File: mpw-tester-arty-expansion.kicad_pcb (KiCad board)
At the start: 4 copper layers, 53.3 x 61.5 mm, 145 parts, among them J1 USB4105-GF-A, J10 61300211121, J11 61300211121, J12 61300211121, J14 61300311121, J15 61300311121, J18 61300411121, J19 61300711121, J20 61300411121, J3 arty_chipKIT_connector, J4 61300211121, J5 61300311121, J6 61300211121, J7 61300211121, J8 61300211121, J9 61300211121, M1 Arty_A7, Q1 DTC014TEBTL, SW1 JS202011JCQN, SW2 JS202011JCQN, SW3 JS202011JCQN, U1 SN74LVC1G125DCKR, U10 TPD4E02B04DQA, U2 FT232HQ, U3 SN74LVC1G125DCKR, U4 MAX811REUS+T, U5 NTS0102DP, U6 MCP4661-103E/ML, U7 Caravel_breakout_PCB, U8 W25Q32FVSS, U9 MIC2211-AAYML-TR, Y1 ABM8G-12.000MHZ-18-D2Y-T, Y2 ECS-2520MVLC-100-BN-TR

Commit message: Update PCB name, bump revision to 1.0.0
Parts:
- moved G*** 2.60 mm to (164.8, 73.8) (x2)
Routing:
- net /CRVL_XCLK: track 27.7 -> 26.8 mm
- net AGND: track 130.1 -> 130.7 mm, vias 61 -> 60
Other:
- board text added: "MPW tester Arty ext."
- board text added: "Rev. 1.0.0"
- board text removed: "MPW tester Arty"
- board text removed: "Rev. 0.0.99"
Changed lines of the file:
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@@
   (title_block
     (title "MPW tester Arty expansion")
-    (date "2022-12-02")
-    (rev "0.0.99")
+    (date "2022-12-12")
+    (rev "1.0.0")
   )
   (layers
@@
   )
   (footprint "antmicro-footprints:antmicro-logo_scaled_12mm_mask" (layer "F.Cu")
-    (at 167.4 73.8)
+    (at 164.8 73.75)
     (attr board_only exclude_from_pos_files exclude_from_bom)
     (fp_text reference "G***" (at 0.6096 -2.0955) (layer "F.SilkS") hide
@@
   )
   (footprint "antmicro-footprints:antmicro-logo_scaled_12mm" (layer "F.Cu")
-    (at 167.4 73.8)
+    (at 164.8 73.75)
     (attr board_only exclude_from_pos_files exclude_from_bom)
     (fp_text reference "G***" (at 0.6096 -2.0955) (layer "F.SilkS") hide
@@
   (gr_line (start 128.1 127.55) (end 125.55 125) (layer "Edge.Cuts") (width 0.1))
   (gr_line (start 174.8 125) (end 163.4 125) (layer "Edge.Cuts") (width 0.1))
-  (gr_text "Rev. 0.0.99" (at 165.1 76.9) (layer "F.Cu")
+  (gr_text "Rev. 1.0.0" (at 162.55 76.75) (layer "F.Cu")
     (effects (font (size 0.85 0.85) (thickness 0.18)) (justify left))
   )
-  (gr_text "MPW tester Arty" (at 165.1 75.5) (layer "F.Cu")
+  (gr_text "MPW tester Arty ext." (at 162.55 75.35) (layer "F.Cu")
     (effects (font (size 0.85 0.85) (thickness 0.18)) (justify left))
   )
@@
     (effects (font (size 0.7 0.7) (thickness 0.15)))
   )
-  (gr_text "Rev. 0.0.99" (at 165.1 76.9) (layer "F.Mask")
+  (gr_text "Rev. 1.0.0" (at 162.55 76.75) (layer "F.Mask")
     (effects (font (size 0.85 0.85) (thickness 0.18)) (justify left))
   )
-  (gr_text "MPW tester Arty" (at 165.1 75.5) (layer "F.Mask")
+  (gr_text "MPW tester Arty ext." (at 162.55 75.35) (layer "F.Mask")
     (effects (font (size 0.85 0.85) (thickness 0.18)) (justify left))
   )
@@
   (via (at 135.7 84.5) (size 0.6) (drill 0.3) (layers "F.Cu" "B.Cu") (net 1))
   (via (at 135.5 78.8) (size 0.6) (drill 0.3) (layers "F.Cu" "B.Cu") (net 1))
-  (via (at 159.9 73.5) (size 0.6) (drill 0.3) (layers "F.Cu" "B.Cu") (net 1))
   (via (at 129.7 84.4) (size 0.6) (drill 0.3) (layers "F.Cu" "B.Cu") (net 1))
   (via (at 134.2 73.6) (size 0.6) (drill 0.3) (layers "F.Cu" "B.Cu") (net 1))
@@
   (segment (start 139.15 109.55) (end 139.2 109.5) (width 0.2) (layer "B.Cu") (net 1))
   (segment (start 130.2 105) (end 130.2 106.43) (width 0.2) (layer "B.Cu") (net 1))
-  (segment (start 159.9 74.4) (end 159.9 73.5) (width 0.2) (layer "B.Cu") (net 1))
   (segment (start 136.65 115.15) (end 136.9 114.9) (width 0.2) (layer "B.Cu") (net 1))
   (segment (start 136.9 125.7) (end 136.9 126.6) (width 0.2) (layer "B.Cu") (net 1))
@@
   (segment (start 163.4 82.2) (end 163.3405 82.2) (width 0.2) (layer "B.Cu") (net 1))
   (segment (start 143.75 89.468) (end 143.75 90.368) (width 0.2) (layer "B.Cu") (net 1))
+  (segment (start 159.9 74.4) (end 159.9 75.9) (width 0.2) (layer "B.Cu") (net 1))
   (segment (start 135.7 83.6) (end 135.7 84.5) (width 0.2) (layer "B.Cu") (net 1))
   (segment (start 146.3 107.2) (end 147 107.75) (width 0.2) (layer "B.Cu") (net 1))
@@
   (segment (start 133.6 123.3) (end 133.6 124.5) (width 0.2) (layer "B.Cu") (net 3))
   (segment (start 123.9 103.9) (end 124.4 103.4) (width 0.2) (layer "B.Cu") (net 3))
-  (segment (start 128.9 75.6) (end 128.9 85.7) (width 0.2) (layer "F.Cu") (net 4))
+  (segment (start 129.4 75.1) (end 128.9 75.6) (width 0.2) (layer "F.Cu") (net 4))
+  (segment (start 158.1 73.5) (end 140.8 73.5) (width 0.2) (layer "F.Cu") (net 4))
   (segment (start 140.8 73.5) (end 139.2 75.1) (width 0.2) (layer "F.Cu") (net 4))
   (segment (start 139.2 75.1) (end 129.4 75.1) (width 0.2) (layer "F.Cu") (net 4))
-  (segment (start 129.4 75.1) (end 128.9 75.6) (width 0.2) (layer "F.Cu") (net 4))
-  (segment (start 158.5 73.5) (end 140.8 73.5) (width 0.2) (layer "F.Cu") (net 4))
+  (segment (start 128.9 75.6) (end 128.9 85.7) (width 0.2) (layer "F.Cu") (net 4))
   (via (at 128.9 85.7) (size 0.6) (drill 0.3) (layers "F.Cu" "B.Cu") (net 4))
-  (via (at 158.5 73.5) (size 0.6) (drill 0.3) (layers "F.Cu" "B.Cu") (net 4))
+  (via (at 158.1 73.5) (size 0.6) (drill 0.3) (layers "F.Cu" "B.Cu") (net 4))
   (segment (start 125.54 94.52) (end 127.98 94.52) (width 0.2) (layer "B.Cu") (net 4))
   (segment (start 127.3 93.7) (end 127.3 86.2) (width 0.2) (layer "B.Cu") (net 4))
@@
   (segment (start 158.9 76.7) (end 157.9 76.7) (width 0.2) (layer "B.Cu") (net 4))
   (segment (start 127.8 85.7) (end 128.9 85.7) (width 0.2) (layer "B.Cu") (net 4))
+  (segment (start 158.5 74.4) (end 158.5 73.9) (width 0.2) (layer "B.Cu") (net 4))
   (segment (start 157.5 76.3) (end 156.6 76.3) (width 0.2) (layer "B.Cu") (net 4))
   (segment (start 128 94.5) (end 128 94.4) (width 0.2) (layer "B.Cu") (net 4))
+  (segment (start 158.5 73.9) (end 158.1 73.5) (width 0.2) (layer "B.Cu") (net 4))
   (segment (start 156.425 74.125) (end 156.7 74.4) (width 0.2) (layer "B.Cu") (net 4))
   (segment (start 128 94.4) (end 127.3 93.7) (width 0.2) (layer "B.Cu") (net 4))
   (segment (start 159.2 76.4) (end 158.9 76.7) (width 0.2) (layer "B.Cu") (net 4))
-  (segment (start 158.5 74.4) (end 158.5 73.5) (width 0.2) (layer "B.Cu") (net 4))
   (segment (start 156.6 76.3) (end 156.425 76.475) (width 0.2) (layer "B.Cu") (net 4))
   (segment (start 127.98 94.52) (end 128 94.5) (width 0.2) (layer "B.Cu") (net 4))
@@
   (via (at 146.95 90.368) (size 0.6) (drill 0.3) (layers "F.Cu" "B.Cu") (net 8))
   (via (at 162.7 84.2) (size 0.6) (drill 0.3) (layers "F.Cu" "B.Cu") (net 8))
-  (via (at 160.5 71.7) (size 0.6) (drill 0.3) (layers "F.Cu" "B.Cu") (net 8))
   (via (at 142 74.4) (size 0.6) (drill 0.3) (layers "F.Cu" "B.Cu") (net 8))
   (via (at 151.75 90.368) (size 0.6) (drill 0.3) (layers "F.Cu" "B.Cu") (net 8))
   (via (at 133.2 76.75) (size 0.6) (drill 0.3) (layers "F.Cu" "B.Cu") (net 8))
+  (via (at 160.7 71) (size 0.6) (drill 0.3) (layers "F.Cu" "B.Cu") (net 8))
   (via (at 153.35 90.368) (size 0.6) (drill 0.3) (layers "F.Cu" "B.Cu") (net 8))
   (segment (start 151.25 108.6) (end 152.3 108.6) (width 0.2) (layer "B.Cu") (net 8))
@@
   (segment (start 153.8 67) (end 152.81 67) (width 0.2) (layer "B.Cu") (net 8))
   (segment (start 171.8 74.205) (end 173.405 74.205) (width 0.2) (layer "B.Cu") (net 8))
+  (segment (start 161.3 71.7) (end 161.3 71.6) (width 0.15) (layer "B.Cu") (net 8))
   (segment (start 148.55 89.468) (end 148.55 90.368) (width 0.2) (layer "B.Cu") (net 8))
   (segment (start 155.25 108.6) (end 155.25 108.15) (width 0.2) (layer "B.Cu") (net 8))
@@
   (segment (start 155.5 107.9) (end 156.2 107.9) (width 0.2) (layer "B.Cu") (net 8))
   (segment (start 142.9 74.4) (end 142 74.4) (width 0.2) (layer "B.Cu") (net 8))
-  (segment (start 161.3 71.7) (end 160.5 71.7) (width 0.2) (layer "B.Cu") (net 8))
+  (segment (start 161.3 71.6) (end 160.7 71) (width 0.15) (layer "B.Cu") (net 8))
   (segment (start 175 73) (end 174.3 73.7) (width 0.2) (layer "B.Cu") (net 8))
   (segment (start 163.3 83.6) (end 162.7 84.2) (width 0.2) (layer "B.Cu") (net 8))
@@
   (segment (start 147.775 84.578) (end 147.775 81.175) (width 0.2) (layer "F.Cu") (net 51))
   (segment (start 147.775 84.578) (end 147.775 86.128) (width 0.2) (layer "F.Cu") (net 51))
-  (segment (start 147.2 77.4) (end 164.1 77.4) (width 0.182) (layer "F.Cu") (net 51))
-  (segment (start 164.455 77.755) (end 164.455 78.9) (width 0.182) (layer "F.Cu") (net 51))
+  (segment (start 163.155 77.6) (end 147.2 77.6) (width 0.182) (layer "F.Cu") (net 51))
+  (segment (start 147.2 77.6) (end 146.94 77.86) (width 0.182) (layer "F.Cu") (net 51))
   (segment (start 146.94 80.34) (end 147.775 81.175) (width 0.2) (layer "F.Cu") (net 51))
-  (segment (start 164.1 77.4) (end 164.455 77.755) (width 0.182) (layer "F.Cu") (net 51))
-  (segment (start 146.94 78.9) (end 146.94 77.66) (width 0.182) (layer "F.Cu") (net 51))
-  (segment (start 146.94 77.66) (end 147.2 77.4) (width 0.182) (layer "F.Cu") (net 51))
+  (segment (start 146.94 77.86) (end 146.94 78.9) (width 0.182) (layer "F.Cu") (net 51))
+  (segment (start 164.455 78.9) (end 163.155 77.6) (width 0.182) (layer "F.Cu") (net 51))
   (segment (start 144.375 76.425) (end 144.4 76.45) (width 0.182) (layer "B.Cu") (net 52))
   (segment (start 144.4 76.45) (end 144.4 78.9) (width 0.182) (layer "B.Cu") (net 52))

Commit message: Removed Arty A7 model
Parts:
- removed M1: Arty_A7, antmicro-footprints:ARTY_A7
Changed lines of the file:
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@@
       ) (layer "F.Mask") (width 0.01) (fill solid))
-  )
-  (footprint "antmicro-footprints:ARTY_A7" (layer "F.Cu")
-    (at 150 100)
-    (property "MPN" "410-319")
-    (property "Manufacturer" "Digilent")
-    (property "Sheetfile" "mpw-tester-arty-expansion.kicad_sch")
-    (property "Sheetname" "")
-    (property "exclude_from_bom" "")
-    (attr exclude_from_bom)
-    (fp_text reference "M1" (at 0 -0.5 unlocked) (layer "F.SilkS") hide
-      (effects (font (size 0.65 0.65) (thickness 0.15)))
-    )
-    (fp_text value "Arty_A7" (at 0 1 unlocked) (layer "F.Fab") hide
-      (effects (font (size 0.65 0.65) (thickness 0.15)))
-    )
-    (model "${ANT3DMDL}/Arty Rev C.stp"
-      (offset (xyz 0.55 24.6 -13.2))
-      (scale (xyz 1 1 1))
-      (rotate (xyz 0 0 90))
-    )
   )
   (footprint "mpw-tester-arty-expansion-footprints:ARTY_A7_SHIELD" locked (layer "F.Cu")

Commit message: Corrected deadbeef signage
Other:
- board text added: "PCB SHA deadbeef"
- board text removed: "PCB SHA deafbeef"
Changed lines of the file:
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@@
     (effects (font (size 0.85 0.85) (thickness 0.18)) (justify left))
   )
-  (gr_text "PCB SHA deafbeef" (at 138.8 126.9) (layer "B.SilkS")
+  (gr_text "PCB SHA deadbeef" (at 138.8 126.9) (layer "B.SilkS")
     (effects (font (size 0.85 0.85) (thickness 0.18)) (justify mirror))
   )

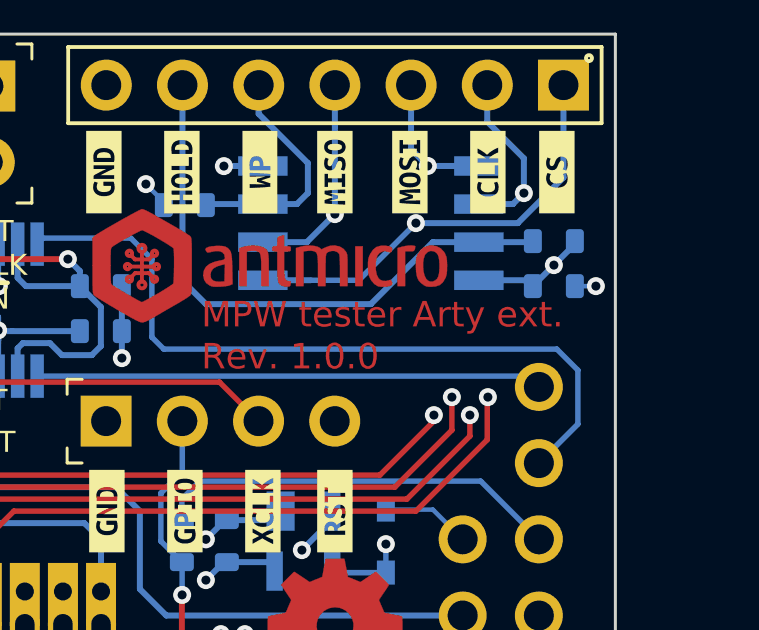
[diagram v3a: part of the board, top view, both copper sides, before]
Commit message: Fix signage
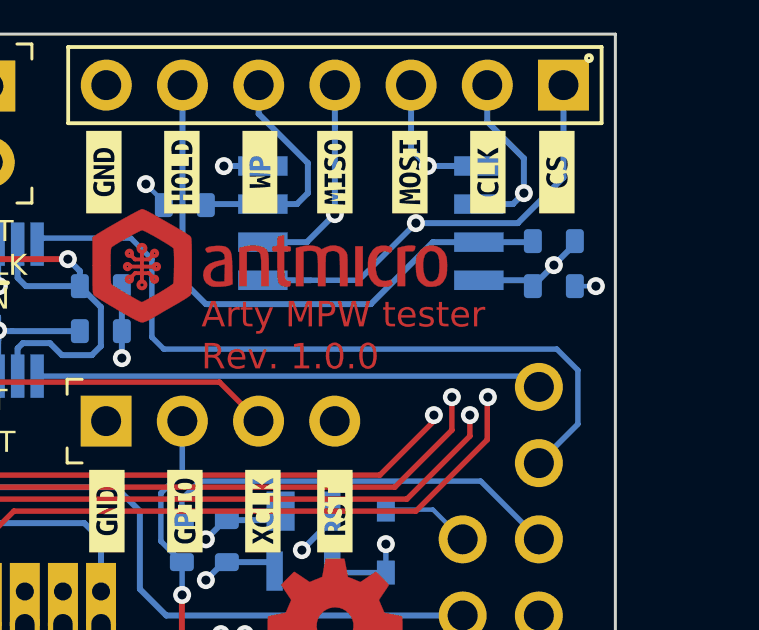
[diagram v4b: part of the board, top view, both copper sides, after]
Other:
- board text added: "Arty MPW tester"
- board text added: "Arty MPW tester Rev. 1.0.0 12/2022"
- board text added: "PCB SHA: deadbeef"
- board text removed: "MPW tester Arty ext."
- board text removed: "PCB SHA deadbeef"
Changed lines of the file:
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@@
       (connect_pads (clearance 0))
       (min_thickness 0.254)
-      (keepout (tracks not_allowed) (vias not_allowed) (pads not_allowed) (copperpour not_allowed) (footprints not_allowed))
+      (keepout (tracks not_allowed) (vias not_allowed) (pads not_allowed ) (copperpour not_allowed) (footprints not_allowed))
       (fill (thermal_gap 0.508) (thermal_bridge_width 0.508))
       (polygon
@@
     (effects (font (size 0.85 0.85) (thickness 0.18)) (justify left))
   )
-  (gr_text "MPW tester Arty ext." (at 162.55 75.35) (layer "F.Cu")
+  (gr_text "Arty MPW tester" (at 162.55 75.35) (layer "F.Cu")
     (effects (font (size 0.85 0.85) (thickness 0.18)) (justify left))
   )
-  (gr_text "PCB SHA deadbeef" (at 138.8 126.9) (layer "B.SilkS")
-    (effects (font (size 0.85 0.85) (thickness 0.18)) (justify mirror))
+  (gr_text "Arty MPW tester\nRev. 1.0.0 12/2022" (at 167.75 108.5 90) (layer "B.SilkS")
+    (effects (font (size 0.85 0.85) (thickness 0.18)) (justify left mirror))
+  )
+  (gr_text "PCB SHA: deadbeef" (at 172.55 108.5 90) (layer "B.SilkS")
+    (effects (font (size 0.85 0.85) (thickness 0.18)) (justify left mirror))
   )
   (gr_text "DIS" (at 131.5 116.6) (layer "F.SilkS")
@@
     (effects (font (size 0.85 0.85) (thickness 0.18)) (justify left))
   )
-  (gr_text "MPW tester Arty ext." (at 162.55 75.35) (layer "F.Mask")
+  (gr_text "Arty MPW tester" (at 162.55 75.35) (layer "F.Mask")
     (effects (font (size 0.85 0.85) (thickness 0.18)) (justify left))
   )
@@
     (connect_pads (clearance 0))
     (min_thickness 0.15)
-    (keepout (tracks allowed) (vias allowed) (pads allowed) (copperpour not_allowed) (footprints allowed))
+    (keepout (tracks allowed) (vias allowed) (pads allowed ) (copperpour not_allowed) (footprints allowed))
     (fill (thermal_gap 0.508) (thermal_bridge_width 0.508))
     (polygon
@@
     (connect_pads (clearance 0))
     (min_thickness 0.15)
-    (keepout (tracks allowed) (vias allowed) (pads allowed) (copperpour not_allowed) (footprints allowed))
+    (keepout (tracks allowed) (vias allowed) (pads allowed ) (copperpour not_allowed) (footprints allowed))
     (fill (thermal_gap 0.508) (thermal_bridge_width 0.508))
     (polygon
